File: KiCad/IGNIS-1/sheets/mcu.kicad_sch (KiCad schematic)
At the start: 11 parts, among them Q1 MMBT3904, U10 ESP32-WROOM DevKit 38p

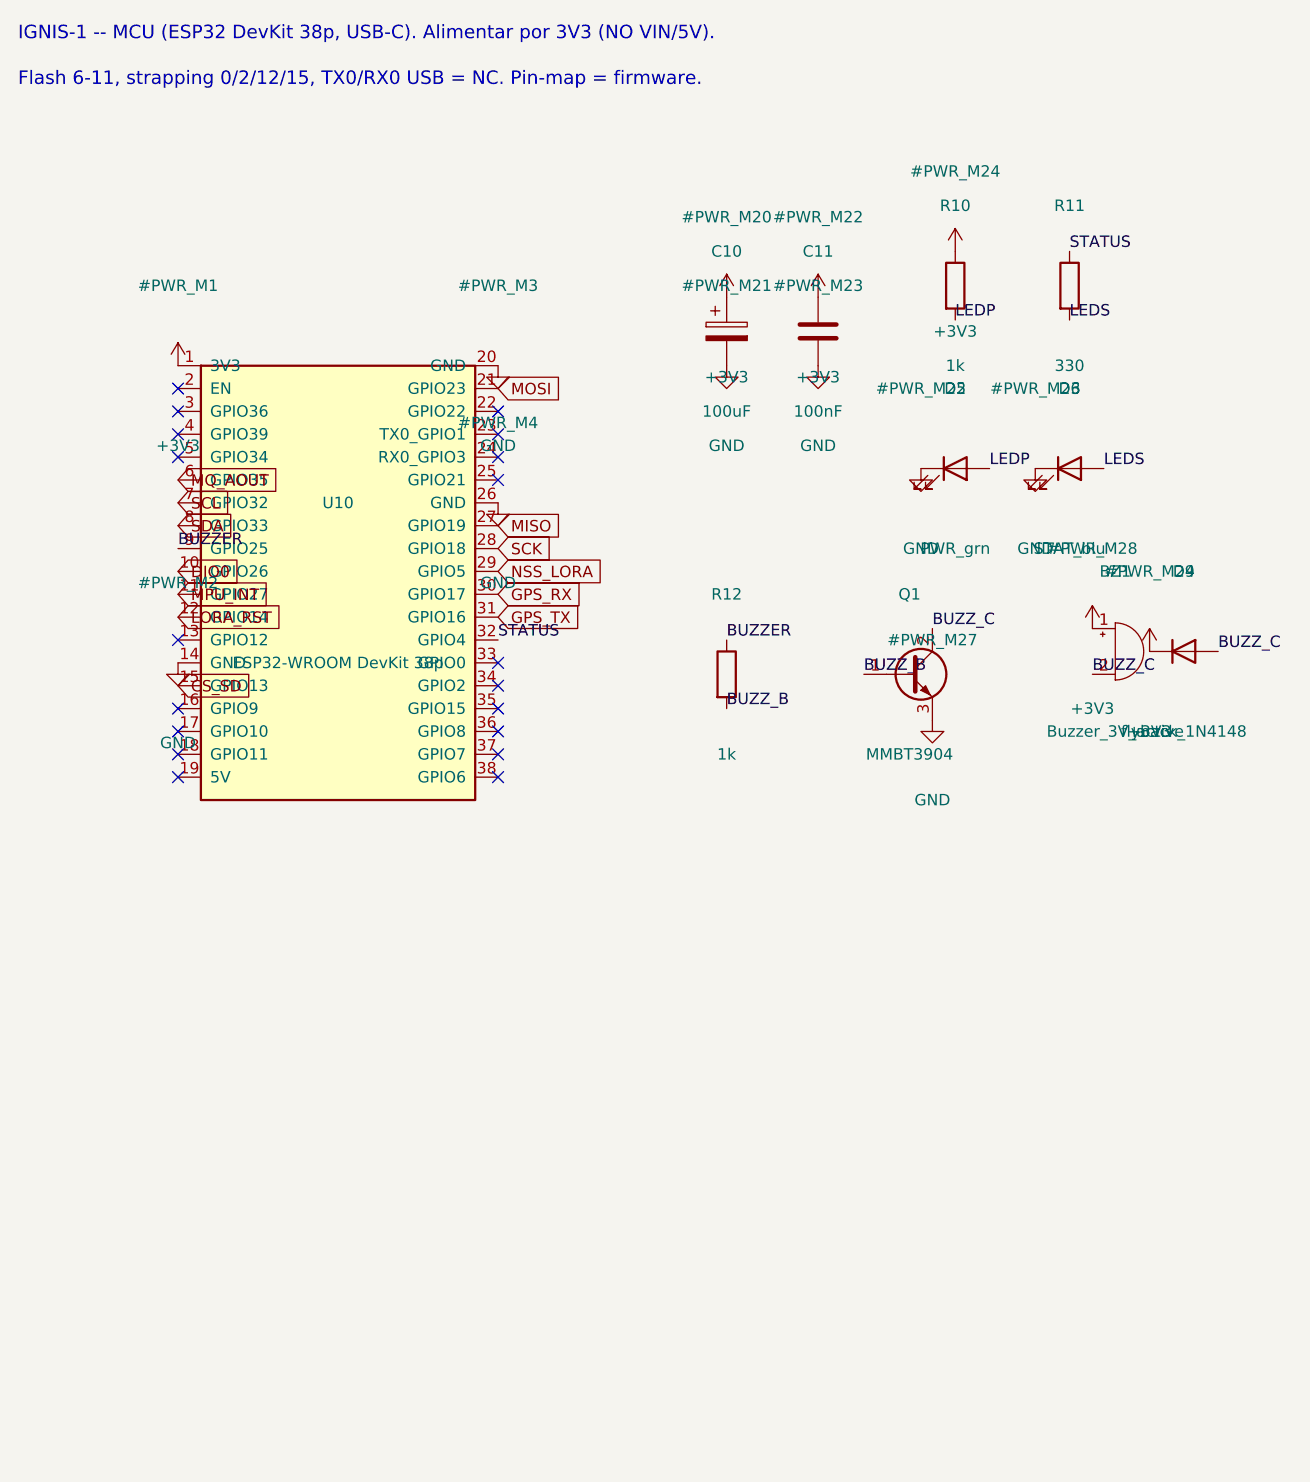
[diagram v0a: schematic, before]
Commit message: Actualizado los boards de IGNIS - separado en 3 boards
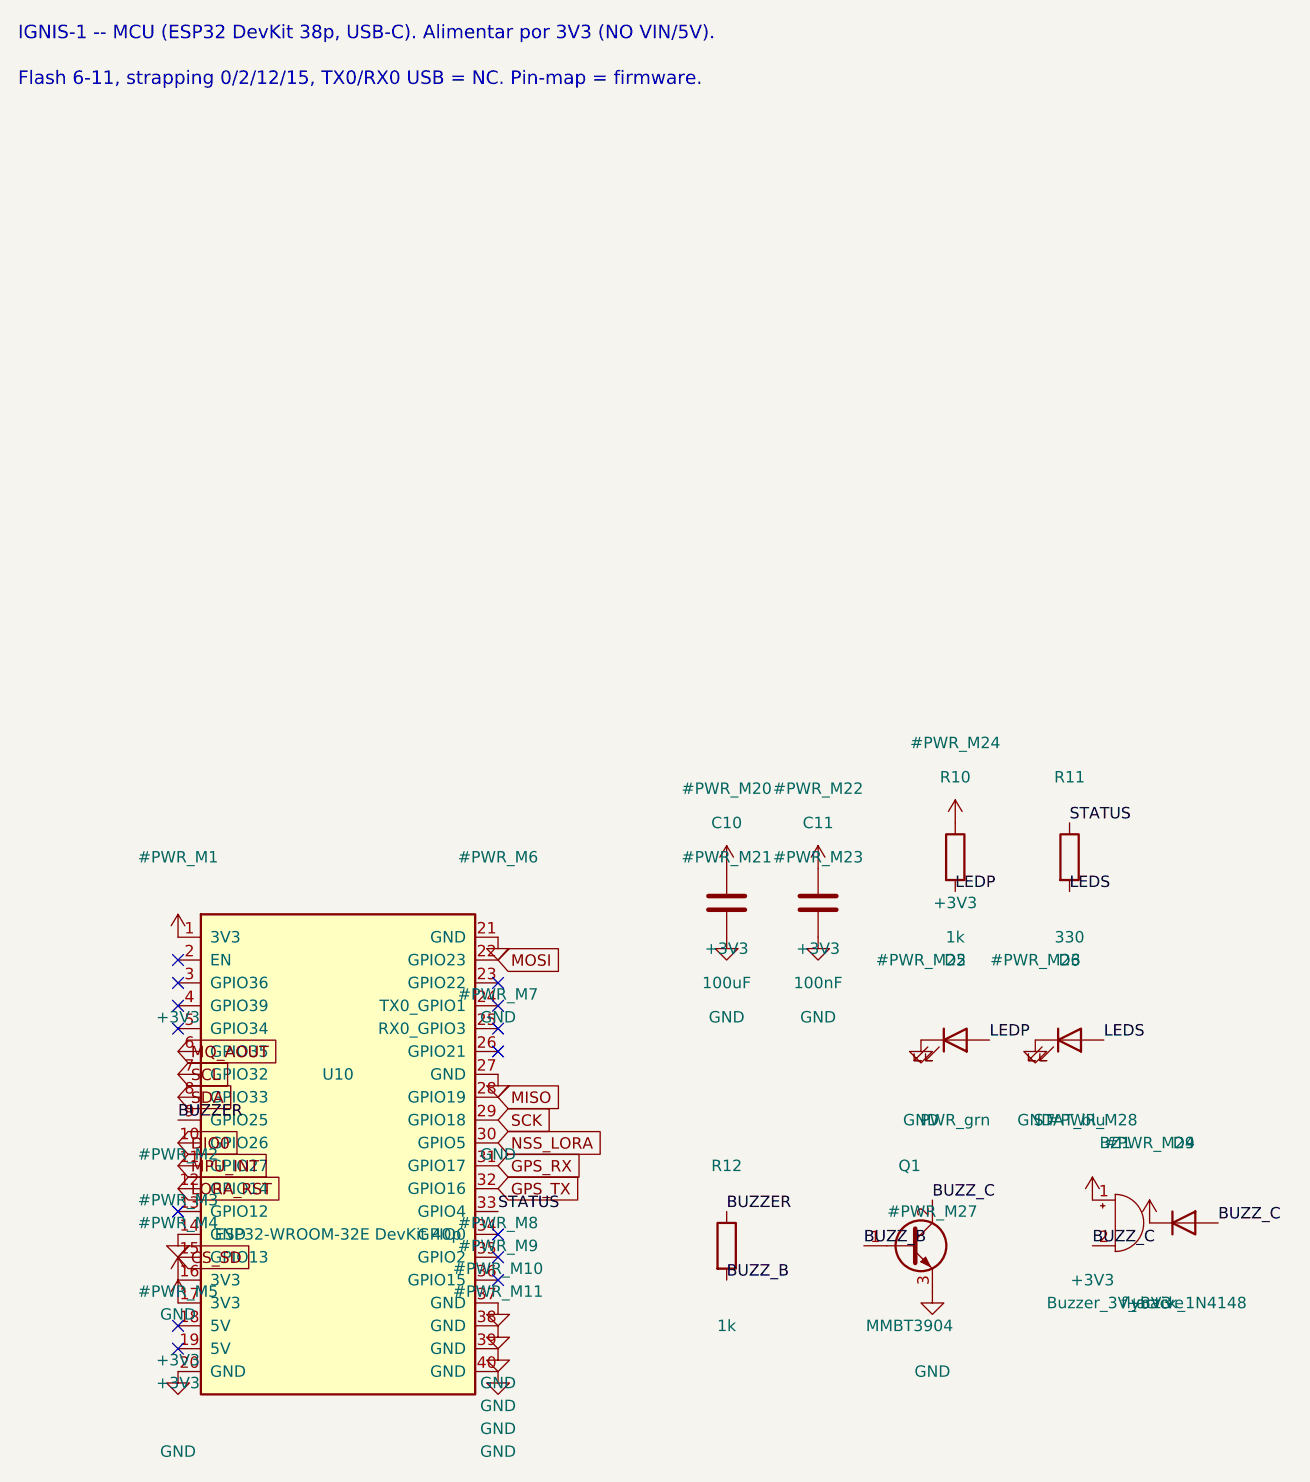
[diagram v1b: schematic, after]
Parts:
- removed C10: 100uF, Capacitor_THT:CP_Radial_D6.3mm_P2.50mm, symbol Device:C_Polarized
- removed U10: ESP32-WROOM DevKit 38p, IGNIS1:ESP32_DevKit_38p, symbol IGNIS1:ESP32_DevKit_38
- added C10: 100uF, Capacitor_SMD:C_1210_3225Metric, symbol Device:C
- added U10: ESP32-WROOM-32E DevKit 40p, IGNIS1:ESP32_DevKit_40p, symbol IGNIS1:ESP32_DevKit_40
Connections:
- net +3V3: now also C10.1, U10.1 (3V3), U10.16 (3V3), U10.17 (3V3)
- net BUZZER: now also U10.9 (GPIO25)
- net CS_SD: now also U10.15 (GPIO13)
- net DIO0: now also U10.10 (GPIO26)
- net GND: now also C10.2, U10.14 (GND), U10.20 (GND), U10.21 (GND), U10.27 (GND), U10.37 (GND), U10.38 (GND), U10.39 (GND), U10.40 (GND)
- net GPS_RX: now also U10.31 (GPIO17)
- net GPS_TX: now also U10.32 (GPIO16)
- net LORA_RST: now also U10.12 (GPIO14)
- net MISO: now also U10.28 (GPIO19)
- net MOSI: now also U10.22 (GPIO23)
- net MPU_INT: now also U10.11 (GPIO27)
- net MQ_AOUT: now also U10.6 (GPIO35)
- net NSS_LORA: now also U10.30 (GPIO5)
- net SCK: now also U10.29 (GPIO18)
- net SCL: now also U10.7 (GPIO32)
- net SDA: now also U10.8 (GPIO33)
- net STATUS: now also U10.33 (GPIO4)
- no-connect marks 19 -> 14
